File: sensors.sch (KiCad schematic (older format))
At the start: 25 parts, among them U2 ADS1120-PW, U5 MPL115A1, U6 MPU-9250

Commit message: updates
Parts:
- added M?: ANEOMETER, symbol Fan
- added R?: R_Small, symbol R_Small
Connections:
- net +3V3: now also R?.1
- new net: M?.1 (+), R?.2
- new net ANEOMETER: M?.2 (-)
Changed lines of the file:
@@
 SPI_MSI
 $Comp
-L GND #PWR053
+L GND #PWR054
 U 1 1 5A776C76
 P 4100 4100
-F 0 "#PWR053" H 4100 3850 50  0001 C CNN
+F 0 "#PWR054" H 4100 3850 50  0001 C CNN
 F 1 "GND" H 4100 3950 50  0000 C CNN
 F 2 "" H 4100 4100 50  0001 C CNN
@@
 $EndComp
 $Comp
-L +3.3V #PWR054
+L +3.3V #PWR055
 U 1 1 5A776C7C
 P 5300 4100
-F 0 "#PWR054" H 5300 3950 50  0001 C CNN
+F 0 "#PWR055" H 5300 3950 50  0001 C CNN
 F 1 "+3.3V" H 5300 4240 50  0000 C CNN
 F 2 "" H 5300 4100 50  0001 C CNN
@@
 $EndComp
 $Comp
-L GND #PWR055
+L GND #PWR056
 U 1 1 5A776C89
 P 4500 4600
-F 0 "#PWR055" H 4500 4350 50  0001 C CNN
+F 0 "#PWR056" H 4500 4350 50  0001 C CNN
 F 1 "GND" H 4500 4450 50  0000 C CNN
 F 2 "" H 4500 4600 50  0001 C CNN
@@
 $EndComp
 $Comp
-L GND #PWR056
+L GND #PWR057
 U 1 1 5A777E2B
 P 1400 2450
-F 0 "#PWR056" H 1400 2200 50  0001 C CNN
+F 0 "#PWR057" H 1400 2200 50  0001 C CNN
 F 1 "GND" H 1400 2300 50  0000 C CNN
 F 2 "" H 1400 2450 50  0000 C CNN
@@
 $EndComp
 $Comp
-L GND #PWR057
+L GND #PWR058
 U 1 1 5A777E31
 P 2100 2450
-F 0 "#PWR057" H 2100 2200 50  0001 C CNN
+F 0 "#PWR058" H 2100 2200 50  0001 C CNN
 F 1 "GND" H 2100 2300 50  0000 C CNN
 F 2 "" H 2100 2450 50  0000 C CNN
@@
 $EndComp
 $Comp
-L GND #PWR058
+L GND #PWR059
 U 1 1 5A777E37
 P 2050 1650
-F 0 "#PWR058" H 2050 1400 50  0001 C CNN
+F 0 "#PWR059" H 2050 1400 50  0001 C CNN
 F 1 "GND" H 2050 1500 50  0000 C CNN
 F 2 "" H 2050 1650 50  0000 C CNN
@@
 SPI_DRDY
 $Comp
-L +3.3V #PWR059
+L +3.3V #PWR060
 U 1 1 5A777E43
 P 2050 3450
-F 0 "#PWR059" H 2050 3300 50  0001 C CNN
+F 0 "#PWR060" H 2050 3300 50  0001 C CNN
 F 1 "+3.3V" H 2050 3590 50  0000 C CNN
 F 2 "" H 2050 3450 50  0000 C CNN
@@
 $EndComp
 $Comp
-L GND #PWR060
+L GND #PWR061
 U 1 1 5A777E49
 P 2050 4600
-F 0 "#PWR060" H 2050 4350 50  0001 C CNN
+F 0 "#PWR061" H 2050 4350 50  0001 C CNN
 F 1 "GND" H 2050 4450 50  0000 C CNN
 F 2 "" H 2050 4600 50  0000 C CNN
@@
 Connection ~ 2050 4600
 $Comp
-L +3.3V #PWR061
+L +3.3V #PWR062
 U 1 1 5A777E65
 P 1450 1650
-F 0 "#PWR061" H 1450 1500 50  0001 C CNN
+F 0 "#PWR062" H 1450 1500 50  0001 C CNN
 F 1 "+3.3V" H 1450 1790 50  0000 C CNN
 F 2 "" H 1450 1650 50  0000 C CNN
@@
 $EndComp
 $Comp
-L GND #PWR062
+L GND #PWR063
 U 1 1 5A777E9E
 P 2600 2450
-F 0 "#PWR062" H 2600 2200 50  0001 C CNN
+F 0 "#PWR063" H 2600 2200 50  0001 C CNN
 F 1 "GND" H 2600 2300 50  0000 C CNN
 F 2 "" H 2600 2450 50  0000 C CNN
@@
 $EndComp
 $Comp
-L GND #PWR063
+L GND #PWR064
 U 1 1 5A777EA4
 P 3300 2450
-F 0 "#PWR063" H 3300 2200 50  0001 C CNN
+F 0 "#PWR064" H 3300 2200 50  0001 C CNN
 F 1 "GND" H 3300 2300 50  0000 C CNN
 F 2 "" H 3300 2450 50  0000 C CNN
@@
 $EndComp
 $Comp
-L GND #PWR064
+L GND #PWR065
 U 1 1 5A777EAA
 P 3250 1650
-F 0 "#PWR064" H 3250 1400 50  0001 C CNN
+F 0 "#PWR065" H 3250 1400 50  0001 C CNN
 F 1 "GND" H 3250 1500 50  0000 C CNN
 F 2 "" H 3250 1650 50  0000 C CNN
@@
 Connection ~ 2850 1650
 $Comp
-L +3.3V #PWR065
+L +3.3V #PWR066
 U 1 1 5A777EBE
 P 2650 1650
-F 0 "#PWR065" H 2650 1500 50  0001 C CNN
+F 0 "#PWR066" H 2650 1500 50  0001 C CNN
 F 1 "+3.3V" H 2650 1790 50  0000 C CNN
 F 2 "" H 2650 1650 50  0000 C CNN
@@
 CS_ADS1120
 $Comp
-L +3.3V #PWR066
+L +3.3V #PWR067
 U 1 1 5A778A93
 P 7350 2450
-F 0 "#PWR066" H 7350 2300 50  0001 C CNN
+F 0 "#PWR067" H 7350 2300 50  0001 C CNN
 F 1 "+3.3V" H 7350 2590 50  0000 C CNN
 F 2 "" H 7350 2450 50  0001 C CNN
@@
 Connection ~ 7450 2700
 $Comp
-L GND #PWR067
+L GND #PWR068
 U 1 1 5A778EB0
 P 7800 2700
-F 0 "#PWR067" H 7800 2450 50  0001 C CNN
+F 0 "#PWR068" H 7800 2450 50  0001 C CNN
 F 1 "GND" H 7800 2550 50  0000 C CNN
 F 2 "" H 7800 2700 50  0001 C CNN
@@
 $EndComp
 $Comp
-L +3.3V #PWR068
+L +3.3V #PWR069
 U 1 1 5A779442
 P 8050 4000
-F 0 "#PWR068" H 8050 3850 50  0001 C CNN
+F 0 "#PWR069" H 8050 3850 50  0001 C CNN
 F 1 "+3.3V" H 8050 4140 50  0000 C CNN
 F 2 "" H 8050 4000 50  0001 C CNN
@@
 $EndComp
 $Comp
-L GND #PWR069
+L GND #PWR070
 U 1 1 5A77947C
 P 8050 4100
-F 0 "#PWR069" H 8050 3850 50  0001 C CNN
+F 0 "#PWR070" H 8050 3850 50  0001 C CNN
 F 1 "GND" H 8050 3950 50  0000 C CNN
 F 2 "" H 8050 4100 50  0001 C CNN
@@
 	8050 3900 8250 3900
 $Comp
-L GND #PWR070
+L GND #PWR071
 U 1 1 5A779778
 P 8450 3900
-F 0 "#PWR070" H 8450 3650 50  0001 C CNN
+F 0 "#PWR071" H 8450 3650 50  0001 C CNN
 F 1 "GND" H 8450 3750 50  0000 C CNN
 F 2 "" H 8450 3900 50  0001 C CNN
@@
 $EndComp
 $Comp
-L GND #PWR071
+L GND #PWR072
 U 1 1 5A77987C
 P 6650 3900
-F 0 "#PWR071" H 6650 3650 50  0001 C CNN
+F 0 "#PWR072" H 6650 3650 50  0001 C CNN
 F 1 "GND" H 6650 3750 50  0000 C CNN
 F 2 "" H 6650 3900 50  0001 C CNN
@@
 $EndComp
 $Comp
-L GND #PWR072
+L GND #PWR073
 U 1 1 5A77AEB3
 P 7350 4600
-F 0 "#PWR072" H 7350 4350 50  0001 C CNN
+F 0 "#PWR073" H 7350 4350 50  0001 C CNN
 F 1 "GND" H 7350 4450 50  0000 C CNN
 F 2 "" H 7350 4600 50  0001 C CNN
@@
 Text GLabel 6650 3400 0    60   Input ~ 0
 SDA
+$Comp
+L Fan M?
+U 1 1 5A76B316
+P 4000 6000
+F 0 "M?" H 4100 6200 50  0000 L CNN
+F 1 "ANEOMETER" H 4100 5900 50  0000 L TNN
+F 2 "" H 4000 6010 50  0001 C CNN
+F 3 "" H 4000 6010 50  0001 C CNN
+	1    4000 6000
+	1    0    0    -1
+$EndComp
+$Comp
+L +3.3V #PWR?
+U 1 1 5A76B491
+P 4000 5500
+F 0 "#PWR?" H 4000 5350 50  0001 C CNN
+F 1 "+3.3V" H 4000 5640 50  0000 C CNN
+F 2 "" H 4000 5500 50  0001 C CNN
+F 3 "" H 4000 5500 50  0001 C CNN
+	1    4000 5500
+	1    0    0    -1
+$EndComp
+Text GLabel 4000 6200 3    60   Input ~ 0
+ANEOMETER
+$Comp
+L R_Small R?
+U 1 1 5A76C08C
+P 4000 5600
+F 0 "R?" H 4030 5620 50  0000 L CNN
+F 1 "R_Small" H 4030 5560 50  0000 L CNN
+F 2 "" H 4000 5600 50  0001 C CNN
+F 3 "" H 4000 5600 50  0001 C CNN
+	1    4000 5600
+	1    0    0    -1
+$EndComp
 $EndSCHEMATC

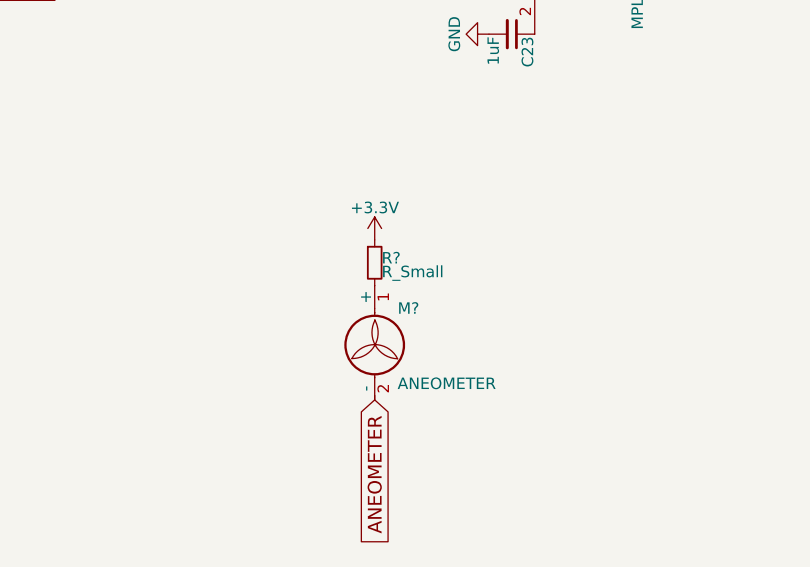
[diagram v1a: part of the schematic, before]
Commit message: basing solar power supply off of openMPPT
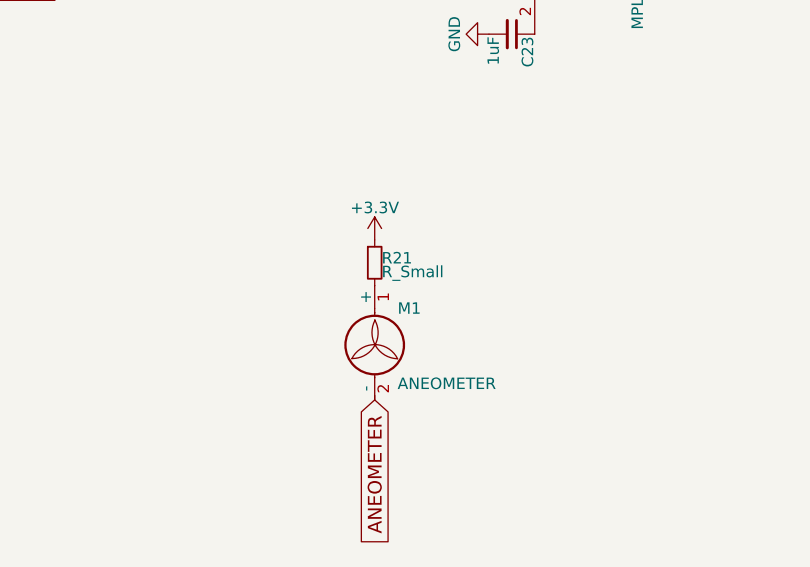
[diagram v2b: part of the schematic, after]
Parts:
- M1: renamed from M?; footprint (none) -> Wire_Connections_Bridges:WireConnection_2.00mmDrill
- R21: renamed from R?; footprint (none) -> Resistors_SMD:R_0603
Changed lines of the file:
@@
 LIBS:nxp_armmcu
 LIBS:sensors
+LIBS:SFUSat-power
 LIBS:weather_station-cache
+LIBS:OpenMPPT-cache
 EELAYER 25 0
 EELAYER END
@@
 SPI_MSI
 $Comp
-L GND #PWR054
+L GND #PWR071
 U 1 1 5A776C76
 P 4100 4100
-F 0 "#PWR054" H 4100 3850 50  0001 C CNN
+F 0 "#PWR071" H 4100 3850 50  0001 C CNN
 F 1 "GND" H 4100 3950 50  0000 C CNN
 F 2 "" H 4100 4100 50  0001 C CNN
@@
 $EndComp
 $Comp
-L +3.3V #PWR055
+L +3.3V #PWR072
 U 1 1 5A776C7C
 P 5300 4100
-F 0 "#PWR055" H 5300 3950 50  0001 C CNN
+F 0 "#PWR072" H 5300 3950 50  0001 C CNN
 F 1 "+3.3V" H 5300 4240 50  0000 C CNN
 F 2 "" H 5300 4100 50  0001 C CNN
@@
 $EndComp
 $Comp
-L GND #PWR056
+L GND #PWR073
 U 1 1 5A776C89
 P 4500 4600
-F 0 "#PWR056" H 4500 4350 50  0001 C CNN
+F 0 "#PWR073" H 4500 4350 50  0001 C CNN
 F 1 "GND" H 4500 4450 50  0000 C CNN
 F 2 "" H 4500 4600 50  0001 C CNN
@@
 $EndComp
 $Comp
-L GND #PWR057
+L GND #PWR074
 U 1 1 5A777E2B
 P 1400 2450
-F 0 "#PWR057" H 1400 2200 50  0001 C CNN
+F 0 "#PWR074" H 1400 2200 50  0001 C CNN
 F 1 "GND" H 1400 2300 50  0000 C CNN
 F 2 "" H 1400 2450 50  0000 C CNN
@@
 $EndComp
 $Comp
-L GND #PWR058
+L GND #PWR075
 U 1 1 5A777E31
 P 2100 2450
-F 0 "#PWR058" H 2100 2200 50  0001 C CNN
+F 0 "#PWR075" H 2100 2200 50  0001 C CNN
 F 1 "GND" H 2100 2300 50  0000 C CNN
 F 2 "" H 2100 2450 50  0000 C CNN
@@
 $EndComp
 $Comp
-L GND #PWR059
+L GND #PWR076
 U 1 1 5A777E37
 P 2050 1650
-F 0 "#PWR059" H 2050 1400 50  0001 C CNN
+F 0 "#PWR076" H 2050 1400 50  0001 C CNN
 F 1 "GND" H 2050 1500 50  0000 C CNN
 F 2 "" H 2050 1650 50  0000 C CNN
@@
 SPI_DRDY
 $Comp
-L +3.3V #PWR060
+L +3.3V #PWR077
 U 1 1 5A777E43
 P 2050 3450
-F 0 "#PWR060" H 2050 3300 50  0001 C CNN
+F 0 "#PWR077" H 2050 3300 50  0001 C CNN
 F 1 "+3.3V" H 2050 3590 50  0000 C CNN
 F 2 "" H 2050 3450 50  0000 C CNN
@@
 $EndComp
 $Comp
-L GND #PWR061
+L GND #PWR078
 U 1 1 5A777E49
 P 2050 4600
-F 0 "#PWR061" H 2050 4350 50  0001 C CNN
+F 0 "#PWR078" H 2050 4350 50  0001 C CNN
 F 1 "GND" H 2050 4450 50  0000 C CNN
 F 2 "" H 2050 4600 50  0000 C CNN
@@
 Connection ~ 2050 4600
 $Comp
-L +3.3V #PWR062
+L +3.3V #PWR079
 U 1 1 5A777E65
 P 1450 1650
-F 0 "#PWR062" H 1450 1500 50  0001 C CNN
+F 0 "#PWR079" H 1450 1500 50  0001 C CNN
 F 1 "+3.3V" H 1450 1790 50  0000 C CNN
 F 2 "" H 1450 1650 50  0000 C CNN
@@
 $EndComp
 $Comp
-L GND #PWR063
+L GND #PWR080
 U 1 1 5A777E9E
 P 2600 2450
-F 0 "#PWR063" H 2600 2200 50  0001 C CNN
+F 0 "#PWR080" H 2600 2200 50  0001 C CNN
 F 1 "GND" H 2600 2300 50  0000 C CNN
 F 2 "" H 2600 2450 50  0000 C CNN
@@
 $EndComp
 $Comp
-L GND #PWR064
+L GND #PWR081
 U 1 1 5A777EA4
 P 3300 2450
-F 0 "#PWR064" H 3300 2200 50  0001 C CNN
+F 0 "#PWR081" H 3300 2200 50  0001 C CNN
 F 1 "GND" H 3300 2300 50  0000 C CNN
 F 2 "" H 3300 2450 50  0000 C CNN
@@
 $EndComp
 $Comp
-L GND #PWR065
+L GND #PWR082
 U 1 1 5A777EAA
 P 3250 1650
-F 0 "#PWR065" H 3250 1400 50  0001 C CNN
+F 0 "#PWR082" H 3250 1400 50  0001 C CNN
 F 1 "GND" H 3250 1500 50  0000 C CNN
 F 2 "" H 3250 1650 50  0000 C CNN
@@
 Connection ~ 2850 1650
 $Comp
-L +3.3V #PWR066
+L +3.3V #PWR083
 U 1 1 5A777EBE
 P 2650 1650
-F 0 "#PWR066" H 2650 1500 50  0001 C CNN
+F 0 "#PWR083" H 2650 1500 50  0001 C CNN
 F 1 "+3.3V" H 2650 1790 50  0000 C CNN
 F 2 "" H 2650 1650 50  0000 C CNN
@@
 CS_ADS1120
 $Comp
-L +3.3V #PWR067
+L +3.3V #PWR084
 U 1 1 5A778A93
 P 7350 2450
-F 0 "#PWR067" H 7350 2300 50  0001 C CNN
+F 0 "#PWR084" H 7350 2300 50  0001 C CNN
 F 1 "+3.3V" H 7350 2590 50  0000 C CNN
 F 2 "" H 7350 2450 50  0001 C CNN
@@
 Connection ~ 7450 2700
 $Comp
-L GND #PWR068
+L GND #PWR085
 U 1 1 5A778EB0
 P 7800 2700
-F 0 "#PWR068" H 7800 2450 50  0001 C CNN
+F 0 "#PWR085" H 7800 2450 50  0001 C CNN
 F 1 "GND" H 7800 2550 50  0000 C CNN
 F 2 "" H 7800 2700 50  0001 C CNN
@@
 $EndComp
 $Comp
-L +3.3V #PWR069
+L +3.3V #PWR086
 U 1 1 5A779442
 P 8050 4000
-F 0 "#PWR069" H 8050 3850 50  0001 C CNN
+F 0 "#PWR086" H 8050 3850 50  0001 C CNN
 F 1 "+3.3V" H 8050 4140 50  0000 C CNN
 F 2 "" H 8050 4000 50  0001 C CNN
@@
 $EndComp
 $Comp
-L GND #PWR070
+L GND #PWR087
 U 1 1 5A77947C
 P 8050 4100
-F 0 "#PWR070" H 8050 3850 50  0001 C CNN
+F 0 "#PWR087" H 8050 3850 50  0001 C CNN
 F 1 "GND" H 8050 3950 50  0000 C CNN
 F 2 "" H 8050 4100 50  0001 C CNN
@@
 	8050 3900 8250 3900
 $Comp
-L GND #PWR071
+L GND #PWR088
 U 1 1 5A779778
 P 8450 3900
-F 0 "#PWR071" H 8450 3650 50  0001 C CNN
+F 0 "#PWR088" H 8450 3650 50  0001 C CNN
 F 1 "GND" H 8450 3750 50  0000 C CNN
 F 2 "" H 8450 3900 50  0001 C CNN
@@
 $EndComp
 $Comp
-L GND #PWR072
+L GND #PWR089
 U 1 1 5A77987C
 P 6650 3900
-F 0 "#PWR072" H 6650 3650 50  0001 C CNN
+F 0 "#PWR089" H 6650 3650 50  0001 C CNN
 F 1 "GND" H 6650 3750 50  0000 C CNN
 F 2 "" H 6650 3900 50  0001 C CNN
@@
 $EndComp
 $Comp
-L GND #PWR073
+L GND #PWR090
 U 1 1 5A77AEB3
 P 7350 4600
-F 0 "#PWR073" H 7350 4350 50  0001 C CNN
+F 0 "#PWR090" H 7350 4350 50  0001 C CNN
 F 1 "GND" H 7350 4450 50  0000 C CNN
 F 2 "" H 7350 4600 50  0001 C CNN
@@
 SDA
 $Comp
-L Fan M?
+L Fan M1
 U 1 1 5A76B316
 P 4000 6000
-F 0 "M?" H 4100 6200 50  0000 L CNN
+F 0 "M1" H 4100 6200 50  0000 L CNN
 F 1 "ANEOMETER" H 4100 5900 50  0000 L TNN
-F 2 "" H 4000 6010 50  0001 C CNN
+F 2 "Wire_Connections_Bridges:WireConnection_2.00mmDrill" H 4000 6010 50  0001 C CNN
 F 3 "" H 4000 6010 50  0001 C CNN
 	1    4000 6000
@@
 $EndComp
 $Comp
-L +3.3V #PWR?
+L +3.3V #PWR091
 U 1 1 5A76B491
 P 4000 5500
-F 0 "#PWR?" H 4000 5350 50  0001 C CNN
+F 0 "#PWR091" H 4000 5350 50  0001 C CNN
 F 1 "+3.3V" H 4000 5640 50  0000 C CNN
 F 2 "" H 4000 5500 50  0001 C CNN
@@
 ANEOMETER
 $Comp
-L R_Small R?
+L R_Small R21
 U 1 1 5A76C08C
 P 4000 5600
-F 0 "R?" H 4030 5620 50  0000 L CNN
+F 0 "R21" H 4030 5620 50  0000 L CNN
 F 1 "R_Small" H 4030 5560 50  0000 L CNN
-F 2 "" H 4000 5600 50  0001 C CNN
+F 2 "Resistors_SMD:R_0603" H 4000 5600 50  0001 C CNN
 F 3 "" H 4000 5600 50  0001 C CNN
 	1    4000 5600

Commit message: i think that's enough for now
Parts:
- R21: value R_Small -> 100kΩ
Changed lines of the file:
@@
 SPI_MSI
 $Comp
-L GND #PWR94
+L GND #PWR083
 U 1 1 5A776C76
 P 4100 4100
-F 0 "#PWR94" H 4100 3850 50  0001 C CNN
+F 0 "#PWR083" H 4100 3850 50  0001 C CNN
 F 1 "GND" H 4100 3950 50  0000 C CNN
 F 2 "" H 4100 4100 50  0001 C CNN
@@
 $EndComp
 $Comp
-L +3.3V #PWR96
+L +3.3V #PWR084
 U 1 1 5A776C7C
 P 5300 4100
-F 0 "#PWR96" H 5300 3950 50  0001 C CNN
+F 0 "#PWR084" H 5300 3950 50  0001 C CNN
 F 1 "+3.3V" H 5300 4240 50  0000 C CNN
 F 2 "" H 5300 4100 50  0001 C CNN
@@
 $EndComp
 $Comp
-L GND #PWR95
+L GND #PWR085
 U 1 1 5A776C89
 P 4500 4600
-F 0 "#PWR95" H 4500 4350 50  0001 C CNN
+F 0 "#PWR085" H 4500 4350 50  0001 C CNN
 F 1 "GND" H 4500 4450 50  0000 C CNN
 F 2 "" H 4500 4600 50  0001 C CNN
@@
 $EndComp
 $Comp
-L GND #PWR83
+L GND #PWR086
 U 1 1 5A777E2B
 P 1400 2450
-F 0 "#PWR83" H 1400 2200 50  0001 C CNN
+F 0 "#PWR086" H 1400 2200 50  0001 C CNN
 F 1 "GND" H 1400 2300 50  0000 C CNN
 F 2 "" H 1400 2450 50  0000 C CNN
@@
 $EndComp
 $Comp
-L GND #PWR88
+L GND #PWR087
 U 1 1 5A777E31
 P 2100 2450
-F 0 "#PWR88" H 2100 2200 50  0001 C CNN
+F 0 "#PWR087" H 2100 2200 50  0001 C CNN
 F 1 "GND" H 2100 2300 50  0000 C CNN
 F 2 "" H 2100 2450 50  0000 C CNN
@@
 $EndComp
 $Comp
-L GND #PWR85
+L GND #PWR088
 U 1 1 5A777E37
 P 2050 1650
-F 0 "#PWR85" H 2050 1400 50  0001 C CNN
+F 0 "#PWR088" H 2050 1400 50  0001 C CNN
 F 1 "GND" H 2050 1500 50  0000 C CNN
 F 2 "" H 2050 1650 50  0000 C CNN
@@
 SPI_DRDY
 $Comp
-L +3.3V #PWR86
+L +3.3V #PWR089
 U 1 1 5A777E43
 P 2050 3450
-F 0 "#PWR86" H 2050 3300 50  0001 C CNN
+F 0 "#PWR089" H 2050 3300 50  0001 C CNN
 F 1 "+3.3V" H 2050 3590 50  0000 C CNN
 F 2 "" H 2050 3450 50  0000 C CNN
@@
 $EndComp
 $Comp
-L GND #PWR87
+L GND #PWR090
 U 1 1 5A777E49
 P 2050 4600
-F 0 "#PWR87" H 2050 4350 50  0001 C CNN
+F 0 "#PWR090" H 2050 4350 50  0001 C CNN
 F 1 "GND" H 2050 4450 50  0000 C CNN
 F 2 "" H 2050 4600 50  0000 C CNN
@@
 Connection ~ 2050 4600
 $Comp
-L +3.3V #PWR84
+L +3.3V #PWR091
 U 1 1 5A777E65
 P 1450 1650
-F 0 "#PWR84" H 1450 1500 50  0001 C CNN
+F 0 "#PWR091" H 1450 1500 50  0001 C CNN
 F 1 "+3.3V" H 1450 1790 50  0000 C CNN
 F 2 "" H 1450 1650 50  0000 C CNN
@@
 $EndComp
 $Comp
-L GND #PWR89
+L GND #PWR092
 U 1 1 5A777E9E
 P 2600 2450
-F 0 "#PWR89" H 2600 2200 50  0001 C CNN
+F 0 "#PWR092" H 2600 2200 50  0001 C CNN
 F 1 "GND" H 2600 2300 50  0000 C CNN
 F 2 "" H 2600 2450 50  0000 C CNN
@@
 $EndComp
 $Comp
-L GND #PWR92
+L GND #PWR093
 U 1 1 5A777EA4
 P 3300 2450
-F 0 "#PWR92" H 3300 2200 50  0001 C CNN
+F 0 "#PWR093" H 3300 2200 50  0001 C CNN
 F 1 "GND" H 3300 2300 50  0000 C CNN
 F 2 "" H 3300 2450 50  0000 C CNN
@@
 $EndComp
 $Comp
-L GND #PWR91
+L GND #PWR094
 U 1 1 5A777EAA
 P 3250 1650
-F 0 "#PWR91" H 3250 1400 50  0001 C CNN
+F 0 "#PWR094" H 3250 1400 50  0001 C CNN
 F 1 "GND" H 3250 1500 50  0000 C CNN
 F 2 "" H 3250 1650 50  0000 C CNN
@@
 Connection ~ 2850 1650
 $Comp
-L +3.3V #PWR90
+L +3.3V #PWR095
 U 1 1 5A777EBE
 P 2650 1650
-F 0 "#PWR90" H 2650 1500 50  0001 C CNN
+F 0 "#PWR095" H 2650 1500 50  0001 C CNN
 F 1 "+3.3V" H 2650 1790 50  0000 C CNN
 F 2 "" H 2650 1650 50  0000 C CNN
@@
 CS_ADS1120
 $Comp
-L +3.3V #PWR98
+L +3.3V #PWR096
 U 1 1 5A778A93
 P 7350 2450
-F 0 "#PWR98" H 7350 2300 50  0001 C CNN
+F 0 "#PWR096" H 7350 2300 50  0001 C CNN
 F 1 "+3.3V" H 7350 2590 50  0000 C CNN
 F 2 "" H 7350 2450 50  0001 C CNN
@@
 Connection ~ 7450 2700
 $Comp
-L GND #PWR100
+L GND #PWR097
 U 1 1 5A778EB0
 P 7800 2700
-F 0 "#PWR100" H 7800 2450 50  0001 C CNN
+F 0 "#PWR097" H 7800 2450 50  0001 C CNN
 F 1 "GND" H 7800 2550 50  0000 C CNN
 F 2 "" H 7800 2700 50  0001 C CNN
@@
 $EndComp
 $Comp
-L +3.3V #PWR101
+L +3.3V #PWR098
 U 1 1 5A779442
 P 8050 4000
-F 0 "#PWR101" H 8050 3850 50  0001 C CNN
+F 0 "#PWR098" H 8050 3850 50  0001 C CNN
 F 1 "+3.3V" H 8050 4140 50  0000 C CNN
 F 2 "" H 8050 4000 50  0001 C CNN
@@
 $EndComp
 $Comp
-L GND #PWR102
+L GND #PWR099
 U 1 1 5A77947C
 P 8050 4100
-F 0 "#PWR102" H 8050 3850 50  0001 C CNN
+F 0 "#PWR099" H 8050 3850 50  0001 C CNN
 F 1 "GND" H 8050 3950 50  0000 C CNN
 F 2 "" H 8050 4100 50  0001 C CNN
@@
 	8050 3900 8250 3900
 $Comp
-L GND #PWR103
+L GND #PWR0100
 U 1 1 5A779778
 P 8450 3900
-F 0 "#PWR103" H 8450 3650 50  0001 C CNN
+F 0 "#PWR0100" H 8450 3650 50  0001 C CNN
 F 1 "GND" H 8450 3750 50  0000 C CNN
 F 2 "" H 8450 3900 50  0001 C CNN
@@
 $EndComp
 $Comp
-L GND #PWR97
+L GND #PWR0101
 U 1 1 5A77987C
 P 6650 3900
-F 0 "#PWR97" H 6650 3650 50  0001 C CNN
+F 0 "#PWR0101" H 6650 3650 50  0001 C CNN
 F 1 "GND" H 6650 3750 50  0000 C CNN
 F 2 "" H 6650 3900 50  0001 C CNN
@@
 $EndComp
 $Comp
-L GND #PWR99
+L GND #PWR0102
 U 1 1 5A77AEB3
 P 7350 4600
-F 0 "#PWR99" H 7350 4350 50  0001 C CNN
+F 0 "#PWR0102" H 7350 4350 50  0001 C CNN
 F 1 "GND" H 7350 4450 50  0000 C CNN
 F 2 "" H 7350 4600 50  0001 C CNN
@@
 $EndComp
 $Comp
-L +3.3V #PWR93
+L +3.3V #PWR0103
 U 1 1 5A76B491
 P 4000 5500
-F 0 "#PWR93" H 4000 5350 50  0001 C CNN
+F 0 "#PWR0103" H 4000 5350 50  0001 C CNN
 F 1 "+3.3V" H 4000 5640 50  0000 C CNN
 F 2 "" H 4000 5500 50  0001 C CNN
@@
 P 4000 5600
 F 0 "R21" H 4030 5620 50  0000 L CNN
-F 1 "R_Small" H 4030 5560 50  0000 L CNN
+F 1 "100kΩ" H 4030 5560 50  0000 L CNN
 F 2 "Resistors_SMD:R_0603" H 4000 5600 50  0001 C CNN
 F 3 "" H 4000 5600 50  0001 C CNN
